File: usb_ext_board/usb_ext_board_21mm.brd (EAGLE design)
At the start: 10 x 30.5 mm, 3 parts

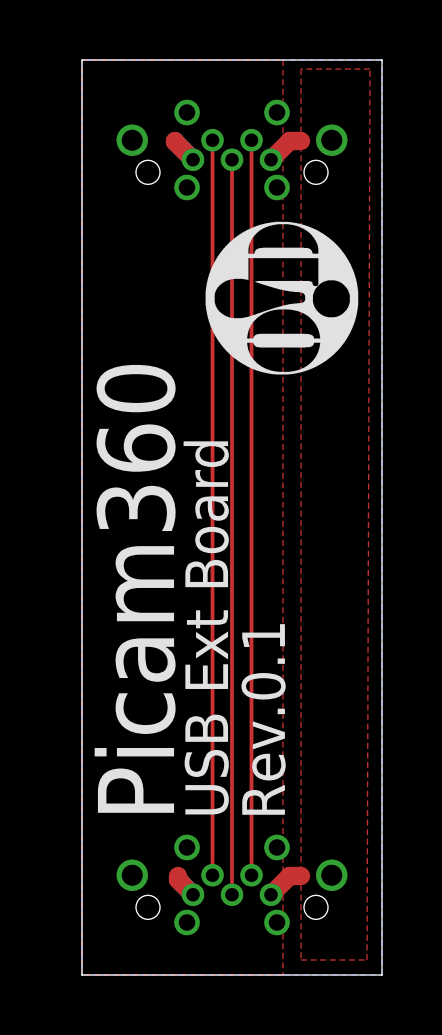
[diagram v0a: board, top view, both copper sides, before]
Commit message: usb_ext_board_21mm
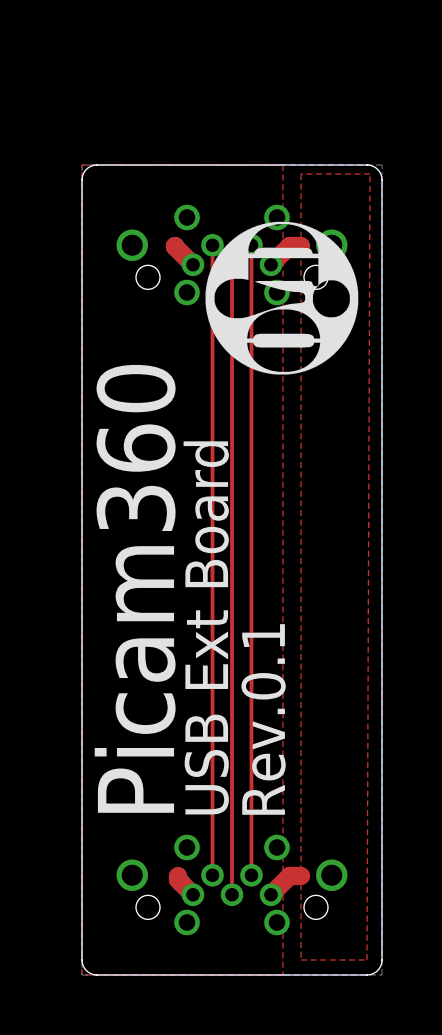
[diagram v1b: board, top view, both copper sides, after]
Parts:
- moved MALE1 3.50 mm to (5.00, 24.0)
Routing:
- net ID: track 24.5 -> 21.0 mm
- net D-: track 24.5 -> 21.0 mm
- net D+: track 24.5 -> 21.0 mm
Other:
- board size 10 x 30.5 mm -> 10 x 27 mm
- board text added: "11.0mm -1.6mm 10.0mm 1.6mm total:21.0mm"
- board text removed: "11.0mm 1.6mm 10.0mm 1.6mm margin:0.3mm total:24.5mm"
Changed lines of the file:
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@@
 <?xml version="1.0" encoding="utf-8"?>
 <!DOCTYPE eagle SYSTEM "eagle.dtd">
-<eagle version="7.5.0">
+<eagle version="8.4.2">
 <drawing>
 <settings>
 <setting alwaysvectorfont="no"/>
+<setting keepoldvectorfont="yes"/>
 <setting verticaltext="up"/>
 </settings>
@@
 <board>
 <plain>
-<wire x1="0" y1="0" x2="10" y2="0" width="0" layer="20"/>
-<wire x1="10" y1="0" x2="10" y2="30.5" width="0" layer="20"/>
-<wire x1="10" y1="30.5" x2="0" y2="30.5" width="0" layer="20"/>
-<wire x1="0" y1="30.5" x2="0" y2="0" width="0" layer="20"/>
+<wire x1="0.5" y1="0" x2="9.5" y2="0" width="0" layer="20"/>
+<wire x1="10" y1="0.5" x2="10" y2="26.5" width="0" layer="20"/>
+<wire x1="9.5" y1="27" x2="0.5" y2="27" width="0" layer="20"/>
 <text x="18.4" y="24.4" size="1.778" layer="48">11.0mm
- 1.6mm
+-1.6mm
 10.0mm
  1.6mm
-margin:0.3mm
-total:24.5mm</text>
+total:21.0mm</text>
 <text x="3.07" y="5.099" size="2.54" layer="21" rot="R90">Picam360</text>
 <text x="4.868" y="5.199" size="1.4224" layer="21" rot="R90">USB Ext Board</text>
 <text x="6.763" y="5.168" size="1.4224" layer="21" rot="R90">Rev.0.1</text>
+<wire x1="0" y1="26.5" x2="0" y2="0.5" width="0" layer="20"/>
+<wire x1="9.5" y1="27" x2="10" y2="26.5" width="0" layer="20" curve="-90"/>
+<wire x1="0" y1="26.5" x2="0.5" y2="27" width="0" layer="20" curve="-90"/>
+<wire x1="0.5" y1="0" x2="0" y2="0.5" width="0" layer="20" curve="-90"/>
+<wire x1="9.5" y1="0" x2="10" y2="0.5" width="0" layer="20" curve="90"/>
 </plain>
 <attributes>
@@
 <param name="dpMaxLengthDifference" value="10mm"/>
 <param name="dpGapFactor" value="2.5"/>
-<param name="checkGrid" value="0"/>
 <param name="checkAngle" value="0"/>
 <param name="checkFont" value="1"/>
 <param name="checkRestrict" value="0"/>
+<param name="checkStop" value="0"/>
 <param name="useDiameter" value="13"/>
 <param name="maxErrors" value="50"/>
@@
 </autorouter>
 <elements>
-<element name="MALE1" library="openblw" package="USB3150-30-130" value="USB-ID" x="5" y="27.5"/>
+<element name="MALE1" library="openblw" package="USB3150-30-130" value="USB-ID" x="5" y="24"/>
 <element name="MALE2" library="openblw" package="USB3150-30-130" value="USB-ID" x="5" y="3"/>
 <element name="LOGO1" library="openblw" package="OHMYDIGIFAB_LOGO" value="" x="6.713" y="22.57" smashed="yes" rot="R90"/>
@@
 <contactref element="MALE1" pad="ID@4"/>
 <contactref element="MALE2" pad="ID@4"/>
-<wire x1="4.35" y1="27.825" x2="4.35" y2="3.325" width="0.127" layer="1"/>
+<wire x1="4.35" y1="24.325" x2="4.35" y2="3.325" width="0.127" layer="1"/>
 </signal>
 <signal name="D+">
 <contactref element="MALE1" pad="D+@3"/>
 <contactref element="MALE2" pad="D+@3"/>
-<wire x1="5" y1="27.175" x2="5" y2="2.675" width="0.127" layer="1"/>
+<wire x1="5" y1="23.675" x2="5" y2="2.675" width="0.127" layer="1"/>
 </signal>
 <signal name="D-">
 <contactref element="MALE1" pad="D-@2"/>
 <contactref element="MALE2" pad="D-@2"/>
-<wire x1="5.65" y1="27.825" x2="5.65" y2="3.325" width="0.127" layer="1"/>
+<wire x1="5.65" y1="24.325" x2="5.65" y2="3.325" width="0.127" layer="1"/>
 </signal>
 <signal name="VCC">
@@
 <contactref element="MALE2" pad="VCC@1"/>
 <polygon width="0.127" layer="1">
-<vertex x="7.3" y="30.2"/>
+<vertex x="7.3" y="26.7"/>
 <vertex x="7.3" y="0.5"/>
 <vertex x="9.5" y="0.5"/>
-<vertex x="9.6" y="30.2"/>
+<vertex x="9.6" y="26.7"/>
 </polygon>
-<wire x1="6.3" y1="27.175" x2="6.925" y2="27.8" width="0.6096" layer="1"/>
-<wire x1="6.925" y1="27.8" x2="7.3" y2="27.8" width="0.6096" layer="1"/>
+<wire x1="6.3" y1="23.675" x2="6.925" y2="24.3" width="0.6096" layer="1"/>
+<wire x1="6.925" y1="24.3" x2="7.3" y2="24.3" width="0.6096" layer="1"/>
 <wire x1="6.3" y1="2.675" x2="6.925" y2="3.3" width="0.6096" layer="1"/>
 <wire x1="6.925" y1="3.3" x2="7.3" y2="3.3" width="0.6096" layer="1"/>
@@
 <contactref element="MALE2" pad="SHELL@7"/>
 <polygon width="0.254" layer="1">
-<vertex x="0" y="30.5"/>
-<vertex x="6.7" y="30.5"/>
+<vertex x="0" y="27"/>
+<vertex x="6.7" y="27"/>
 <vertex x="6.7" y="0"/>
 <vertex x="0" y="0"/>
 </polygon>
 <polygon width="0.254" layer="16">
-<vertex x="10" y="30.5"/>
-<vertex x="0" y="30.5"/>
+<vertex x="10" y="27"/>
+<vertex x="0" y="27"/>
 <vertex x="0" y="0"/>
 <vertex x="10" y="0"/>
 </polygon>
-<wire x1="3.1" y1="27.775" x2="3.7" y2="27.175" width="0.6096" layer="16"/>
-<wire x1="3.1" y1="27.8" x2="3.1" y2="27.775" width="0.6096" layer="16"/>
-<wire x1="3.7" y1="27.175" x2="3.1" y2="27.775" width="0.6096" layer="1"/>
-<wire x1="3.1" y1="27.775" x2="3.1" y2="27.8" width="0.6096" layer="1"/>
+<wire x1="3.1" y1="24.275" x2="3.7" y2="23.675" width="0.6096" layer="16"/>
+<wire x1="3.1" y1="24.3" x2="3.1" y2="24.275" width="0.6096" layer="16"/>
+<wire x1="3.7" y1="23.675" x2="3.1" y2="24.275" width="0.6096" layer="1"/>
+<wire x1="3.1" y1="24.275" x2="3.1" y2="24.3" width="0.6096" layer="1"/>
 <wire x1="3.7" y1="2.675" x2="3.3" y2="3.075" width="0.6096" layer="16"/>
 <wire x1="3.3" y1="3.075" x2="3.3" y2="3.1" width="0.6096" layer="16"/>
